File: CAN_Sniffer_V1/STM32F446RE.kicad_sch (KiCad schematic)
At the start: 1 part, among them U3 STM32F446RETx

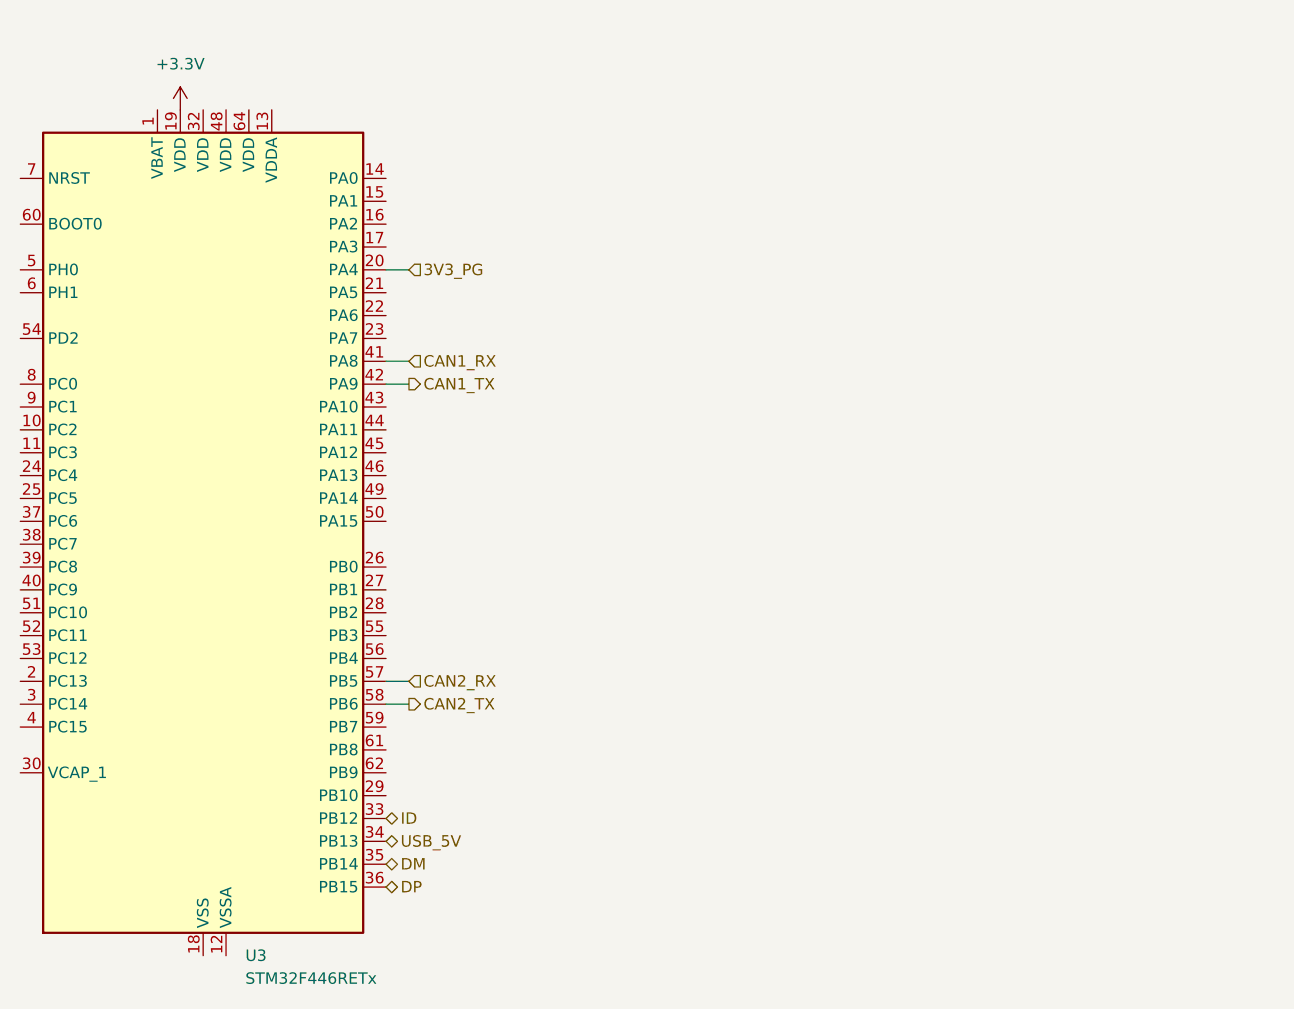
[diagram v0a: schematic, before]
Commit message: changed power schematics and STM32, added MicroSD card connector and LCD display
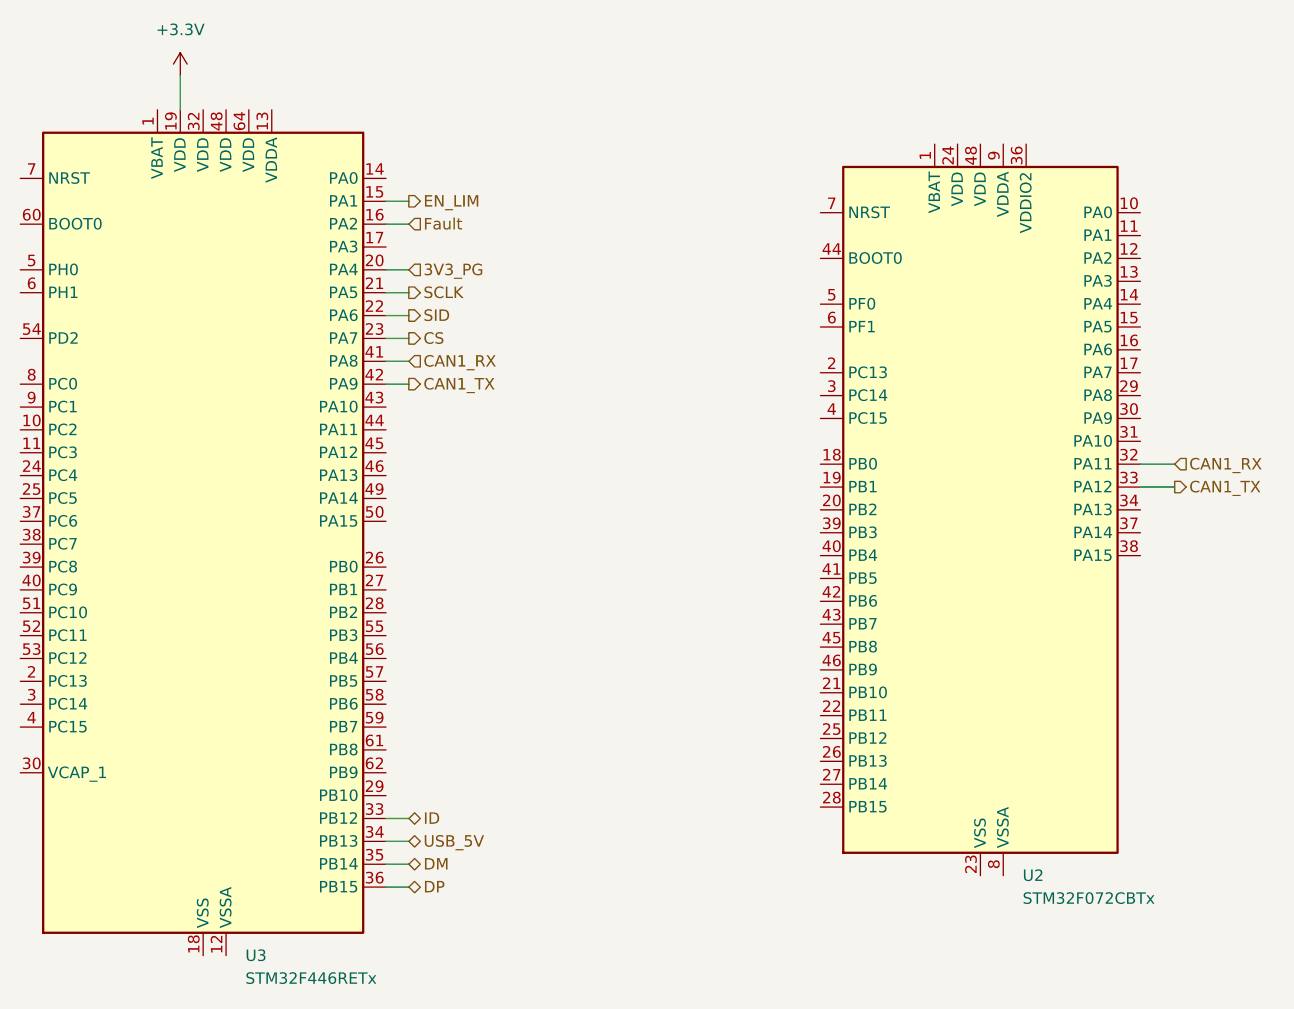
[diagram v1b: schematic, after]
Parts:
- added U2: STM32F072CBTx, Package_QFP:LQFP-48_7x7mm_P0.5mm, symbol MCU_ST_STM32F0:STM32F072CBTx
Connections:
- net CAN1_RX: now also U2.32 (PA11)
- net CAN1_TX: now also U2.33 (PA12)
- net EN_LIM: now reaches U3.15 (PA1)
- net Fault: now reaches U3.16 (PA2)
- net SCLK: now reaches U3.21 (PA5)
- net SID: now reaches U3.22 (PA6)
- net CS: now reaches U3.23 (PA7)
- net CAN2_RX: no longer names the net of U3.57 (PB5)
- net CAN2_TX: no longer names the net of U3.58 (PB6)
- new net: U2.23 (VSS), U2.35 (VSS), U2.47 (VSS)
